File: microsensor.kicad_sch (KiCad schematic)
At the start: 22 parts, among them J1 ARM SWD, Q1 IRLML2244TRPBF, SW1 Control, U1 HDC2080, U2 RV-3028-C7, U3 NORA B206, Y1 32768

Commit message: v0.4 Switched to 4 layers Minor re-routing Changed button to smaller model Added mounting holes Added some missing 3d models
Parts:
- SW1: footprint Button_Switch_SMD:SW_SPST_Omron_B3FS-100xP -> footprints:B3U-1000P

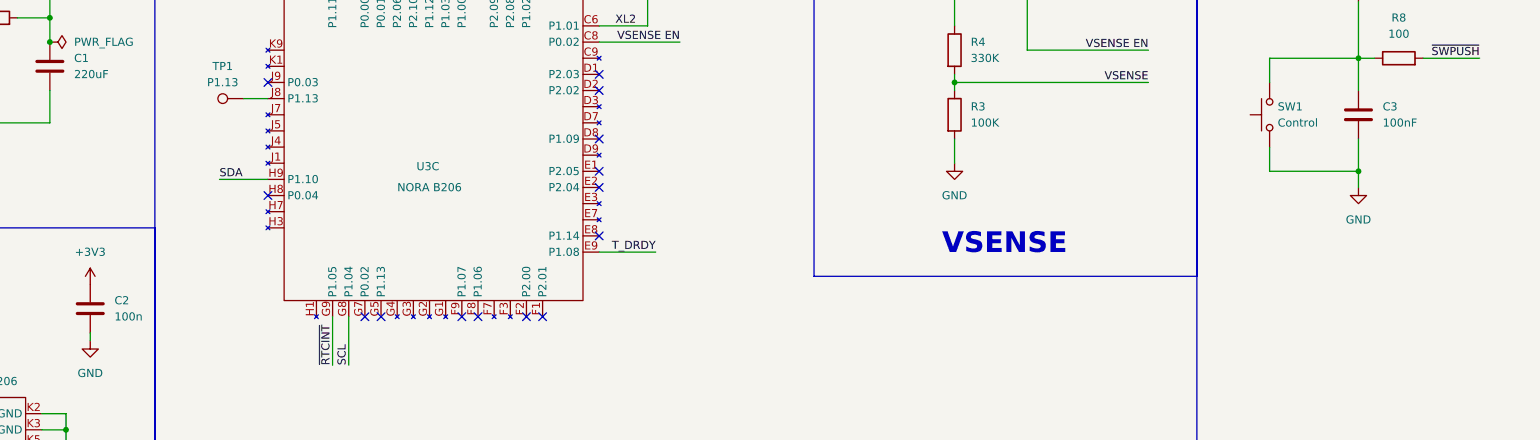
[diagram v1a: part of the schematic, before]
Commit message: Update BOM, add DigiKey list with parts
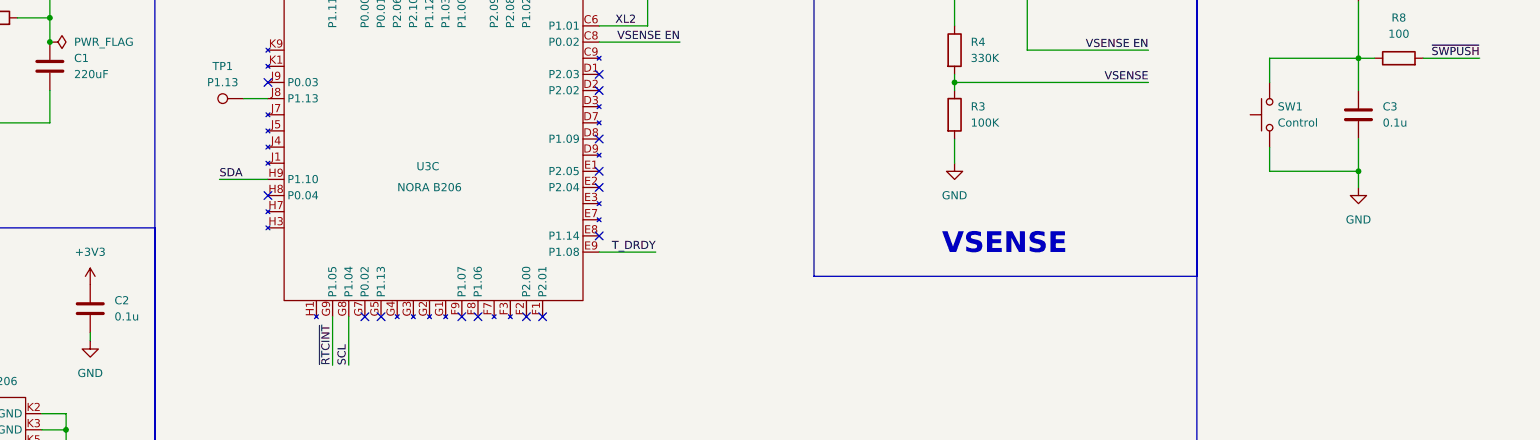
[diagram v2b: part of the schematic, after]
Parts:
- C2: value 100n -> 0.1u
- C3: value 100nF -> 0.1u
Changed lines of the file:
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@@
 			)
 		)
-		(property "Value" "100n"
+		(property "Value" "0.1u"
 			(at 57.15 138.4299 0)
 			(show_name no)
@@
 			)
 		)
-		(property "Value" "100nF"
+		(property "Value" "0.1u"
 			(at 256.54 107.9499 0)
 			(show_name no)
